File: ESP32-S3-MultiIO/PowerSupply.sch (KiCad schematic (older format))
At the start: 5 parts

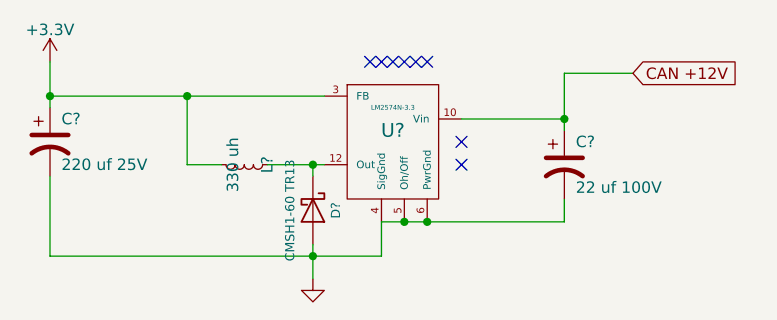
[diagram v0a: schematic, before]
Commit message: Completed ESP32-S3-MultiIO (LCC SMINI replacement).
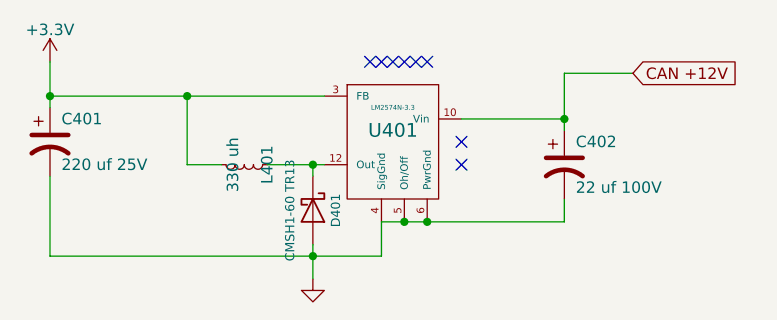
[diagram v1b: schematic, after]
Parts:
- gave numbers to parts that had none: 5
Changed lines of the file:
@@
 LIBS:tbd62x83a
 LIBS:USBLC6-2SC6
+LIBS:mechanical
 LIBS:ESP32-S3-MultiIO-cache
 EELAYER 25 0
@@
 $Descr USLetter 11000 8500
 encoding utf-8
-Sheet 4 4
+Sheet 4 7
 Title "ESP32 S3 Multifunction Board"
 Date ""
@@
 $EndDescr
 $Comp
-L LM2574HVM-5.0 U?
+L LM2574HVM-5.0 U401
 U 1 1 632C8425
 P 5200 2800
-F 0 "U?" H 5200 2850 60  0000 C CNN
+F 0 "U401" H 5200 2850 60  0000 C CNN
 F 1 "LM2574N-3.3" H 5200 2950 21  0000 C CNN
 F 2 "SOIC_Wide:SOIC-14_7.4x8.7mm_Pitch1.27mm" H 5200 2800 60  0001 C CNN
@@
 $EndComp
 $Comp
-L CP1 C?
+L CP1 C402
 U 1 1 632C8426
 P 5950 2900
-F 0 "C?" H 6000 3000 50  0000 L CNN
+F 0 "C402" H 6000 3000 50  0000 L CNN
 F 1 "22 uf 100V" H 6000 2800 50  0000 L CNN
 F 2 "Capacitors_SMD:CP_Elec_8x10" H 5950 2900 60  0001 C CNN
@@
 $EndComp
 $Comp
-L CP1 C?
+L CP1 C401
 U 1 1 632C8427
 P 3700 2800
-F 0 "C?" H 3750 2900 50  0000 L CNN
+F 0 "C401" H 3750 2900 50  0000 L CNN
 F 1 "220 uf 25V" H 3750 2700 50  0000 L CNN
 F 2 "Capacitors_SMD:CP_Elec_8x10" H 3700 2800 60  0001 C CNN
@@
 $EndComp
 $Comp
-L L_Small L?
+L L_Small L401
 U 1 1 632C8428
 P 4550 2900
-F 0 "L?" H 4550 3000 50  0000 C CNN
+F 0 "L401" H 4550 3000 50  0000 C CNN
 F 1 "330 uh" H 4550 2850 50  0000 C CNN
 F 2 "SRN1060:SRN1060" H 4550 2900 60  0001 C CNN
@@
 $EndComp
 $Comp
-L D_Schottky D?
+L D_Schottky D401
 U 1 1 632C8429
 P 4850 3100
-F 0 "D?" H 4850 3200 40  0000 C CNN
+F 0 "D401" H 4850 3200 40  0000 C CNN
 F 1 "CMSH1-60 TR13" H 4850 3000 40  0000 C CNN
 F 2 "Diodes_SMD:D_SMB" H 4850 3100 60  0001 C CNN
@@
 $EndComp
 $Comp
-L GND #PWR?
+L GND #PWR402
 U 1 1 632C842A
 P 4850 3400
-F 0 "#PWR?" H 4850 3400 30  0001 C CNN
+F 0 "#PWR402" H 4850 3400 30  0001 C CNN
 F 1 "GND" H 4850 3330 30  0001 C CNN
 F 2 "" H 4850 3400 60  0000 C CNN
@@
 NoConn ~ 5100 2450
 $Comp
-L +3.3V #PWR?
+L +3.3V #PWR401
 U 1 1 632C842B
 P 3700 2450
-F 0 "#PWR?" H 3700 2300 50  0001 C CNN
+F 0 "#PWR401" H 3700 2300 50  0001 C CNN
 F 1 "+3.3V" H 3700 2590 50  0000 C CNN
 F 2 "" H 3700 2450 50  0001 C CNN
